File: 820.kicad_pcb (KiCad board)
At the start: 2 copper layers, 48 x 105 mm, 123 parts, among them J1 PJ301BM, J10 PJ301BM, J2 PJ301BM, J4 PJ301BM, J5 PJ301BM, J6 PJ301BM, J7 PJ301BM, J8 PJ301BM, J9 PJ301BM, P1 CONN_02X05, P2 CONN_01X03, P3 CONN_01X08, P4 CONN_01X08, Q1 2SC4207, Q2 PMBT2369, Q3 MMBF4391LT1G, Q4 2SA1832, Q5 PMBT2369, SW1 SPDT, SW2 DP6T-ALPHA-SR2511, U1 OPA2180, U2 TL072-, U3 TL072-, U4 TL072-, U5 TA75S558F

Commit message: mostly placed
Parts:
- moved C5 128.0 mm to (134.0, 43.2)
- moved R8 97.9 mm to (95.5, 74.2)
- moved R6 97.3 mm to (98.5, 74.2)
- moved R5 96.8 mm to (101.5, 74.2)
- moved R2 96.4 mm to (104.5, 74.2)
- moved R1 96.1 mm to (107.5, 74.2)
- moved C2 95.2 mm to (115.2, 74.8), turned to 180 degrees
- moved C4 90.0 mm to (129.8, 81.0)
- moved C1 89.3 mm to (119.8, 80.8)
- moved R3 88.7 mm to (96.0, 83.5), turned to 180 degrees
- moved VR1 86.9 mm to (95.0, 78.8)
- moved C3 86.2 mm to (114.2, 83.8), turned to 90 degrees
- moved D3 85.5 mm to (96.0, 86.8)
- moved C18 80.5 mm to (115.8, 89.5), turned to 180 degrees
- moved R35 80.4 mm to (134.8, 91.8), turned to 180 degrees
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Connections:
- VR10 pad 1: +12V -> Net-(R35-Pad2)
- VR10 pad 3: Net-(R35-Pad2) -> +12V
- VR9 pad 1: +10V -> -10V
- VR9 pad 3: -10V -> +10V
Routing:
- net Net-(C17-Pad2): track 18.1 -> 85.1 mm
- net Net-(C19-Pad2): track 0.00 -> 23.8 mm
- net Net-(J4-Pad3): track 0.00 -> 12.5 mm
- net Net-(D5-Pad2): track 0.00 -> 12.4 mm
- net Net-(C13-Pad2): track 0.00 -> 9.82 mm
- net Net-(J5-Pad3): track 0.00 -> 8.72 mm
- net Net-(C14-Pad1): track 0.00 -> 7.23 mm
- net Net-(Q5-Pad2): track 0.00 -> 4.87 mm
- net Net-(C14-Pad2): track 15.5 -> 19.9 mm
- net Net-(R13-Pad1): track 0.00 -> 4.37 mm
- net Net-(Q1-Pad2): track 0.00 -> 3.85 mm
- net SYNC: track 0.00 -> 3.54 mm
- net Net-(C17-Pad1): track 0.00 -> 3.52 mm
- net Net-(R10-Pad1): track 0.00 -> 3.08 mm
- net Net-(Q2-Pad3): track 0.00 -> 3.02 mm
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
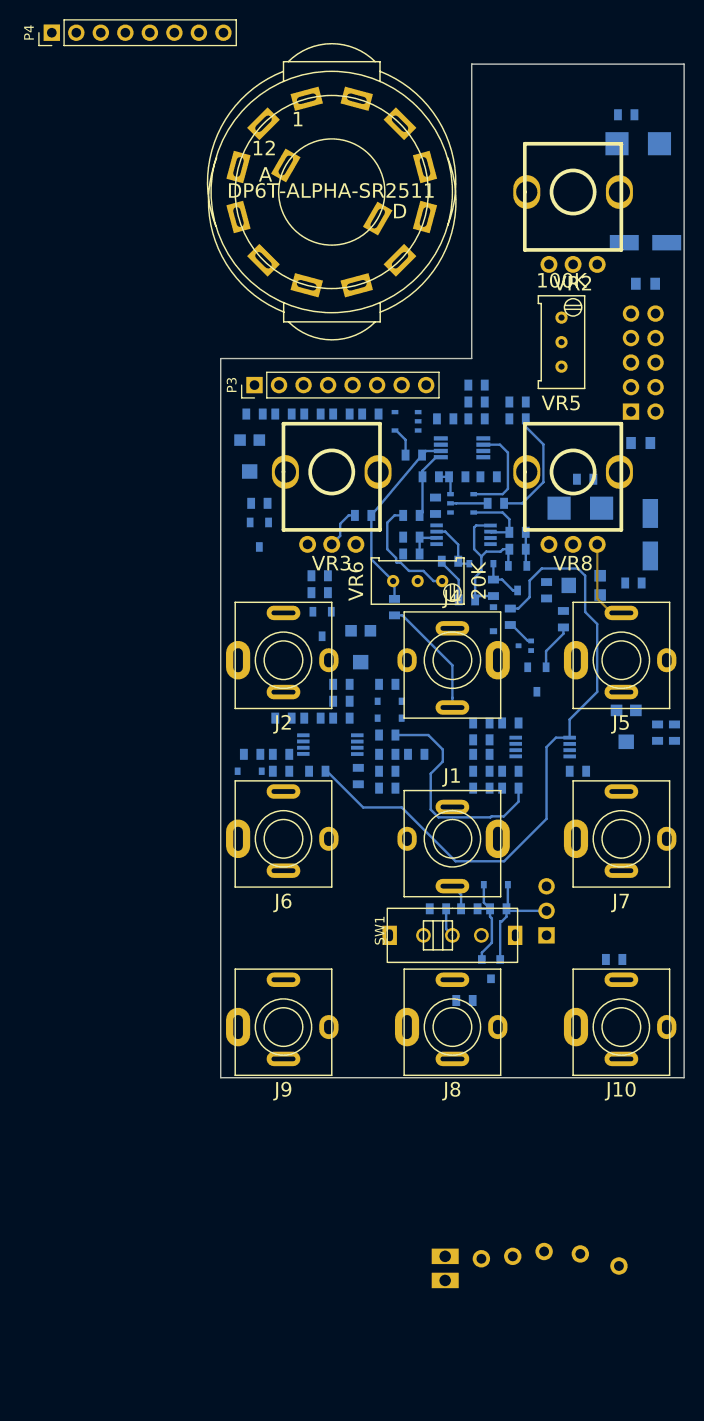
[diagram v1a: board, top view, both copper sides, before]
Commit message: routed, except for rotary switch on separate daughter board
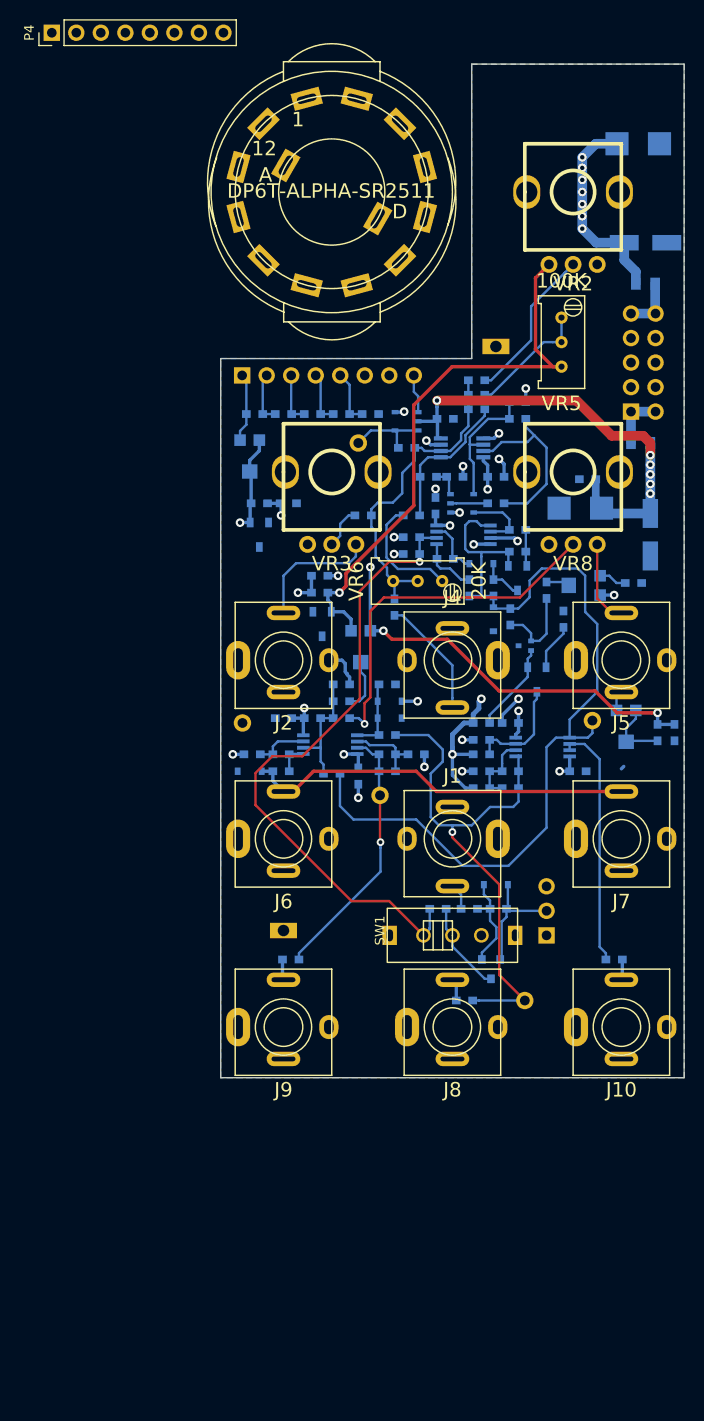
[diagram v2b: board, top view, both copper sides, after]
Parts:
- C1, C10, C13, C14, C15, C16, C17, C18, C19, C2, C20, C3, C4, C5, C6, C7, C8, C9: footprint MyModules:SM0603-C-JRL -> MyModules:SM0603-C-MURATA
- P3: moved to B.Cu
- R1, R10, R11, R12, R13, R15, R16, R17, R18, R19, R2, R20, R21, R22, R23, R24, R25, R26, R27, R28, R29, R3, R30, R31, R32, R33, R34, R35, R36, R37, R38, R39, R4, R40, R41, R42, R43, R44, R45, R46, R47, R48, R49, R5, R50, R6, R7, R8, R9, TC1: footprint MyModules:SM0603-R-JRL -> MyModules:SM0603-R-YAGEO
- moved TP1 94.4 mm to (120.5, 67.2)
- moved TP3 85.5 mm to (106.2, 77.2)
- moved TP5 63.0 mm to (94.2, 106.2)
- moved TP4 56.1 mm to (130.5, 106.0)
- moved TP7 54.7 mm to (108.5, 113.8)
- moved C5 53.3 mm to (99.0, 83.5)
- moved TP2 39.9 mm to (98.5, 127.8)
- moved TP6 26.9 mm to (123.5, 135.0)
- moved R50 20.4 mm to (99.2, 130.8), turned to 180 degrees
- moved P3 7.68 mm to (103.1, 70.2), turned to 270 degrees
- moved R26 1.52 mm to (103.5, 111.5)
- moved R29 1.27 mm to (117.8, 92.2), turned to 90 degrees
- moved R10 1.06 mm to (111.2, 77.8)
- moved C14 1.00 mm to (118.5, 73.8)
- moved C1 0.75 mm to (120.5, 80.8)
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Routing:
- net +12V: track 0.00 -> 215.1 mm, vias 0 -> 16
- net -12V: track 0.00 -> 163.5 mm, vias 0 -> 10
- net +10V: track 0.00 -> 116.9 mm, vias 0 -> 6
- net SYNC: track 3.54 -> 66.3 mm, vias 0 -> 1
- net -10V: track 0.00 -> 59.3 mm, vias 0 -> 1
- net /PULSE: track 0.00 -> 49.9 mm
- net Net-(R23-Pad1): track 0.00 -> 37.6 mm, vias 0 -> 1
- net Net-(C19-Pad2): track 23.8 -> 55.0 mm, vias 0 -> 1
- net GND: track 0.00 -> 28.7 mm, vias 0 -> 16
- net Net-(C20-Pad2): track 0.00 -> 27.3 mm, vias 0 -> 1
- net Net-(R40-Pad1): track 0.00 -> 25.4 mm
- net Net-(R12-Pad1): track 0.00 -> 16.2 mm
- net Net-(C14-Pad2): track 19.9 -> 33.9 mm
- net Net-(J2-Pad3): track 0.00 -> 13.4 mm
- net Net-(R15-Pad1): track 0.00 -> 12.7 mm
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- added copper zone on B.Cu, net GND
- added copper zone on In2.Cu, net GND
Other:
- copper layers 2 -> 4
- net class Default: via_dia 0.6 -> 0.8
- net class POWER added: clearance 0.2, trace_width 0.35, via_dia 0.9, via_drill 0.45

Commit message: separated rotary switch daughter board, finished routing
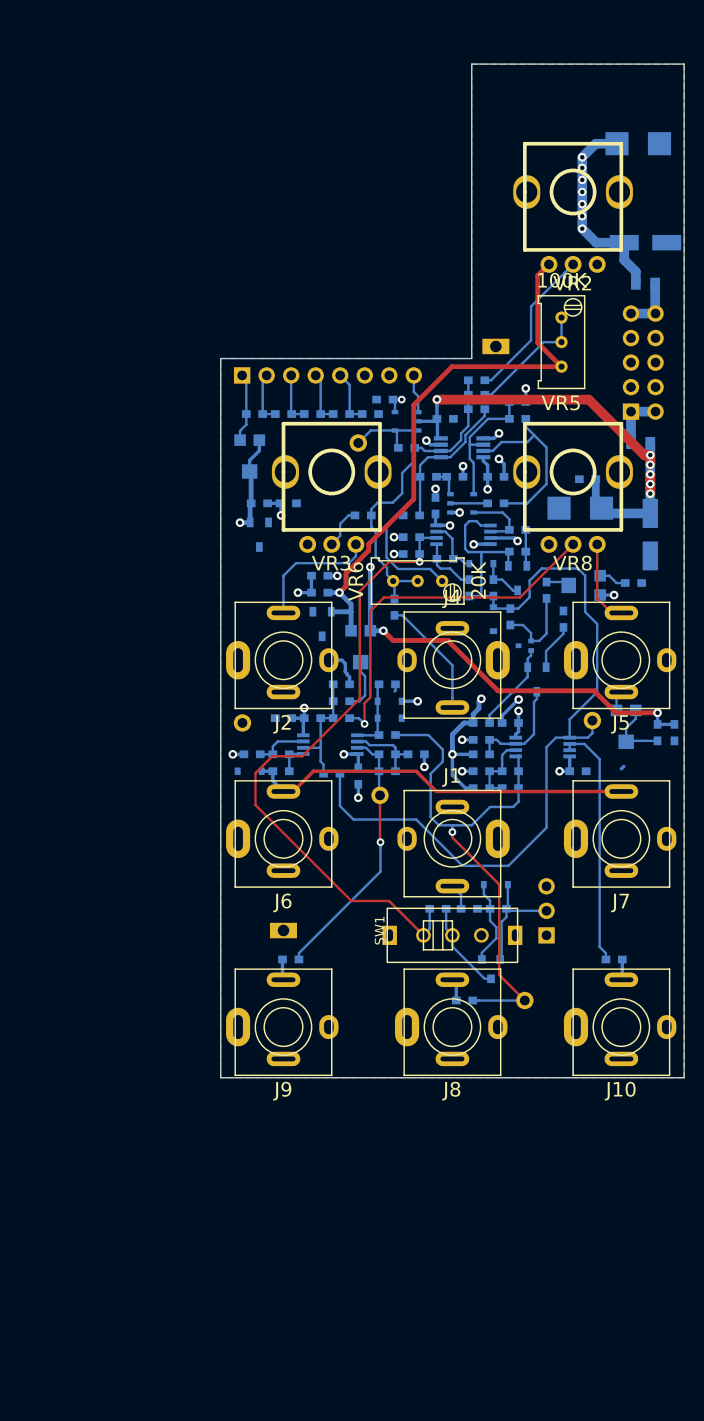
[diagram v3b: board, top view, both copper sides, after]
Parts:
- removed P4: CONN_01X08, Pin_Headers:Pin_Header_Straight_1x08_Pitch2.54mm
- removed SW2: DP6T-ALPHA-SR2511, MyModules:SR2511-ALPHA
- added C21: 0.1µ, MyModules:SM0603-C-MURATA, B.Cu at (109.0, 72.8)
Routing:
- net +10V: track 116.9 -> 122.3 mm
- net +12V: track 215.1 -> 217.6 mm
- net -12V: track 163.5 -> 165.9 mm
- net GND: track 28.7 -> 29.3 mm
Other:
- rule pad_to_mask_clearance: 0.2 -> 0.05

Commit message: bit of tweaking, need to start placing references
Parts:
- moved C14 1.03 mm to (118.2, 74.8)
- moved R12 0.79 mm to (118.2, 71.5)
- moved R15 0.79 mm to (118.2, 73.0)
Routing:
- net GND: track 29.3 -> 45.5 mm, vias 16 -> 25
- net Net-(C15-Pad1): track 14.1 -> 12.9 mm
- net Net-(R15-Pad1): track 12.7 -> 13.9 mm
- net Net-(R12-Pad1): track 16.2 -> 17.2 mm
- net Net-(C14-Pad2): track 33.9 -> 33.0 mm
- net -12V: track 165.9 -> 166.6 mm
- net Net-(C15-Pad2): track 18.8 -> 19.5 mm
- net Net-(C14-Pad1): track 15.1 -> 14.5 mm
- net +10V: track 122.3 -> 121.7 mm

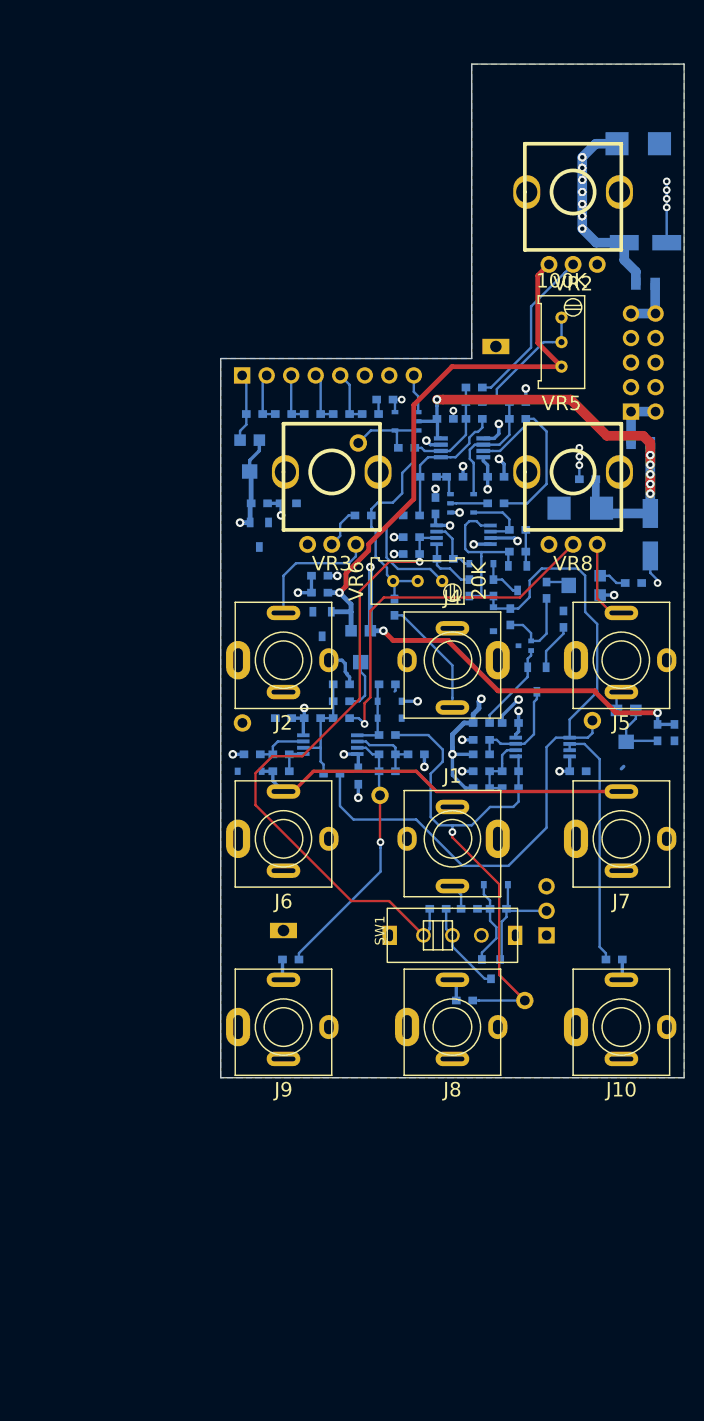
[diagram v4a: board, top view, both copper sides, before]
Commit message: arranged silk screen references
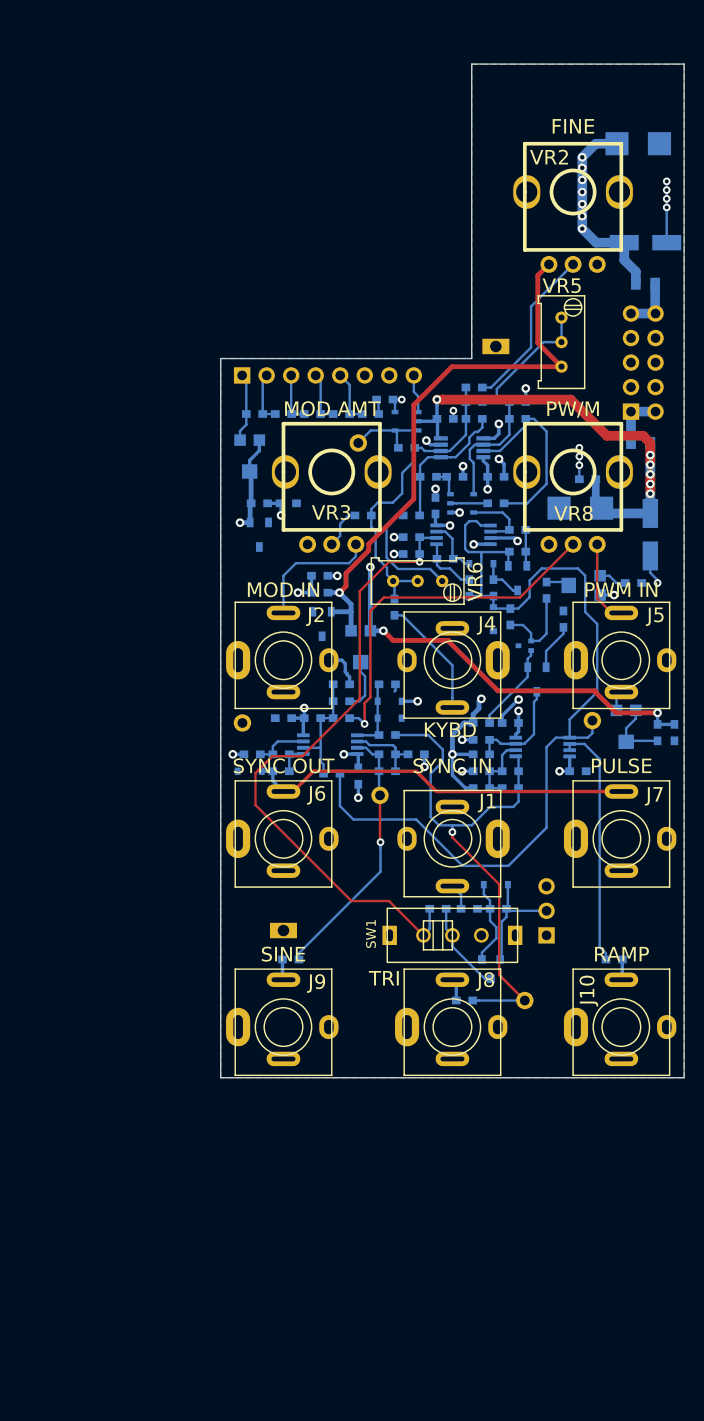
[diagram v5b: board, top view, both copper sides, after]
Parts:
- added G***: LOGO, w_logo:Logo_silk_OSHW_6x6mm, B.Cu at (133.5, 137.2)
- added G***: LOGO, Logos:80_logo_7.5mm, B.Cu at (104.2, 125.2)
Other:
- board text added: "FINE"
- board text added: "KYBD"
- board text added: "MOD AMT"
- board text added: "MOD IN"
- board text added: "PULSE"
- board text added: "PW/M"
- board text added: "PWM IN"
- board text added: "RAMP"
- board text added: "SINE"
- board text added: "SYNC IN"
- board text added: "SYNC OUT"
- board text added: "TRI"
- board text added: "r1.0 08/2018"
- board text added: "system80.net"

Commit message: fixed incorrect pin on switch board: 9 was connected instead of 8
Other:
- board text added: "5% ADJ"
- board text added: "50% ADJ"
- board text added: "820 VCO"
- board text added: "OCT ADJ"
- board text added: "TRI SYM"
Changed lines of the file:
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@@
     (links 244)
     (no_connects 0)
-    (area 91.949999 37.949999 140.050001 143.049993)
+    (area 87.617857 37.949999 141.285 143.049993)
     (thickness 1.6)
-    (drawings 118)
+    (drawings 123)
     (tracks 706)
     (zones 0)
@@
   (page A4)
   (layers
-    (0 F.Cu signal)
-    (1 In1.Cu mixed)
+    (0 F.Cu signal hide)
+    (1 In1.Cu mixed hide)
     (2 In2.Cu power)
     (31 B.Cu signal)
@@
     (35 F.Paste user)
     (36 B.SilkS user)
-    (37 F.SilkS user)
+    (37 F.SilkS user hide)
     (38 B.Mask user)
     (39 F.Mask user)
     (40 Dwgs.User user)
     (41 Cmts.User user)
-    (42 Eco1.User user)
+    (42 Eco1.User user hide)
     (43 Eco2.User user)
     (44 Edge.Cuts user)
@@
     (pad_to_paste_clearance -0.05)
     (aux_axis_origin 0 0)
-    (visible_elements 7FFFF77F)
+    (visible_elements 7FFFB7FF)
     (pcbplotparams
-      (layerselection 0x01400_00000000)
-      (usegerberextensions false)
-      (excludeedgelayer false)
+      (layerselection 0x010f0_80000007)
+      (usegerberextensions true)
+      (excludeedgelayer true)
       (linewidth 0.200000)
       (plotframeref false)
@@
       (plotinvisibletext false)
       (padsonsilk false)
-      (subtractmaskfromsilk false)
-      (outputformat 3)
+      (subtractmaskfromsilk true)
+      (outputformat 1)
       (mirror false)
       (drillshape 0)
@@
     (descr "Through hole straight pin header, 1x08, 2.54mm pitch, single row")
     (tags "Through hole pin header THT 1x08 2.54mm single row")
-    (fp_text reference P3 (at 0 11.22 270) (layer B.SilkS)
+    (fp_text reference P3 (at 1.95 8.91 360) (layer B.SilkS)
       (effects (font (size 1 1) (thickness 0.15)) (justify mirror))
     )
@@
       (effects (font (size 0.6096 0.6096) (thickness 0.1524)) (justify mirror))
     )
-    (fp_text value 1N4148 (at 0 -1.905 90) (layer B.SilkS) hide
-      (effects (font (size 1 1) (thickness 0.15)) (justify mirror))
+    (fp_text value 1N4148 (at 0 0 90) (layer B.SilkS) hide
+      (effects (font (size 0.6 0.6) (thickness 0.15)) (justify mirror))
     )
     (fp_line (start 0.508 0.508) (end 0.508 -0.508) (layer B.SilkS) (width 0.15))
@@
       (effects (font (size 0.6096 0.6096) (thickness 0.1524)) (justify mirror))
     )
-    (fp_text value 1N4148 (at 0 -1.905 180) (layer B.SilkS) hide
-      (effects (font (size 1 1) (thickness 0.15)) (justify mirror))
+    (fp_text value 1N4148 (at 0 -0.25 180) (layer B.SilkS) hide
+      (effects (font (size 0.6 0.6) (thickness 0.15)) (justify mirror))
     )
     (fp_line (start 0.508 0.508) (end 0.508 -0.508) (layer B.SilkS) (width 0.15))
@@
       (effects (font (size 0.6096 0.6096) (thickness 0.1524)) (justify mirror))
     )
-    (fp_text value MMBF4391LT1G (at 0.0635 0) (layer B.SilkS) hide
-      (effects (font (size 0.8128 0.8128) (thickness 0.1524)) (justify mirror))
+    (fp_text value MMBF4391LT1G (at 1 -0.5) (layer B.SilkS) hide
+      (effects (font (size 0.6 0.6) (thickness 0.15)) (justify mirror))
     )
     (fp_line (start 1.27 -0.762) (end -1.3335 -0.762) (layer B.SilkS) (width 0.127))
@@
     (descr http://www.bourns.com/docs/Product-Datasheets/TC33.pdf)
     (tags "Bourns, trimmer")
-    (fp_text reference VR1 (at 3 -1.75) (layer B.SilkS)
-      (effects (font (size 1 1) (thickness 0.15)) (justify mirror))
+    (fp_text reference VR1 (at -1.4 3.15 180) (layer B.SilkS)
+      (effects (font (size 0.8 0.8) (thickness 0.15)) (justify mirror))
     )
     (fp_text value 100 (at 0.3 3.3) (layer B.Fab) hide
@@
     (descr http://www.bourns.com/docs/Product-Datasheets/TC33.pdf)
     (tags "Bourns, trimmer")
-    (fp_text reference VR7 (at -0.1 3.05) (layer B.SilkS)
-      (effects (font (size 1 1) (thickness 0.15)) (justify mirror))
+    (fp_text reference VR7 (at 2.6 -3.15) (layer B.SilkS)
+      (effects (font (size 0.8 0.8) (thickness 0.15)) (justify mirror))
     )
     (fp_text value 22K (at 0.3 3.3) (layer B.Fab) hide
@@
     (descr http://www.bourns.com/docs/Product-Datasheets/TC33.pdf)
     (tags "Bourns, trimmer")
-    (fp_text reference VR9 (at 0.25 -3.25) (layer B.SilkS)
-      (effects (font (size 1 1) (thickness 0.15)) (justify mirror))
+    (fp_text reference VR9 (at 2.6 0 90) (layer B.SilkS)
+      (effects (font (size 0.8 0.8) (thickness 0.15)) (justify mirror))
     )
     (fp_text value 100K (at 0.3 3.3) (layer B.Fab) hide
@@
     (descr http://www.bourns.com/docs/Product-Datasheets/TC33.pdf)
     (tags "Bourns, trimmer")
-    (fp_text reference VR10 (at -2.7 -0.1 360) (layer B.SilkS)
-      (effects (font (size 1 1) (thickness 0.15)) (justify mirror))
+    (fp_text reference VR10 (at -2.5 0 360) (layer B.SilkS)
+      (effects (font (size 0.8 0.8) (thickness 0.15)) (justify mirror))
     )
-    (fp_text value 10K (at 0.3 3.3 270) (layer B.Fab) hide
-      (effects (font (size 1 1) (thickness 0.15)) (justify mirror))
+    (fp_text value 10K (at 0 -0.25 360) (layer B.Fab) hide
+      (effects (font (size 0.6 0.6) (thickness 0.15)) (justify mirror))
     )
     (fp_line (start 0.25 1) (end 0.25 0.25) (layer B.SilkS) (width 0.15))
@@
     (at 96 83.5 180)
     (attr smd)
-    (fp_text reference R3 (at 0 1.4 180) (layer B.SilkS)
+    (fp_text reference R3 (at 0 1.1 180) (layer B.SilkS)
       (effects (font (size 0.6096 0.6096) (thickness 0.1524)) (justify mirror))
     )
@@
     (at 127.5 95.5 270)
     (attr smd)
-    (fp_text reference R34 (at 0 -1.2 270) (layer B.SilkS)
+    (fp_text reference R34 (at 0 1.1 270) (layer B.SilkS)
       (effects (font (size 0.6096 0.6096) (thickness 0.1524)) (justify mirror))
     )
@@
     (at 99 83.5)
     (attr smd)
-    (fp_text reference C5 (at 0 1.4) (layer B.SilkS)
+    (fp_text reference C5 (at 0.3 1.1) (layer B.SilkS)
       (effects (font (size 0.6096 0.6096) (thickness 0.1524)) (justify mirror))
     )
@@
       (xy 0.869885 1.763705) (xy 0.912192 1.766322) (xy 1.059509 1.7637)) (layer B.SilkS) (width 0.01))
   )
+  (gr_text "5%\nADJ" (at 134.7 110.4) (layer B.SilkS)
+    (effects (font (size 0.8 0.8) (thickness 0.15)) (justify left mirror))
+  )
+  (gr_text "50%\nADJ" (at 107.5 94.6) (layer B.SilkS)
+    (effects (font (size 0.8 0.8) (thickness 0.15)) (justify left mirror))
+  )
+  (gr_text "TRI\nSYM" (at 131.3 95.2) (layer B.SilkS)
+    (effects (font (size 0.8 0.8) (thickness 0.15)) (justify left mirror))
+  )
+  (gr_text "OCT\nADJ" (at 99.2 77.1) (layer B.SilkS)
+    (effects (font (size 0.8 0.8) (thickness 0.15)) (justify left mirror))
+  )
+  (gr_text "820 VCO" (at 128.75 40.5) (layer B.SilkS)
+    (effects (font (size 2 2) (thickness 0.35)) (justify mirror))
+  )
   (gr_text system80.net (at 107 132.25) (layer B.SilkS)
